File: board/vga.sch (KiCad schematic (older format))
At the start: 12 parts, among them P501 DE-15, P502 DE-15, U501 TCA9617A, U502 TCA9617A

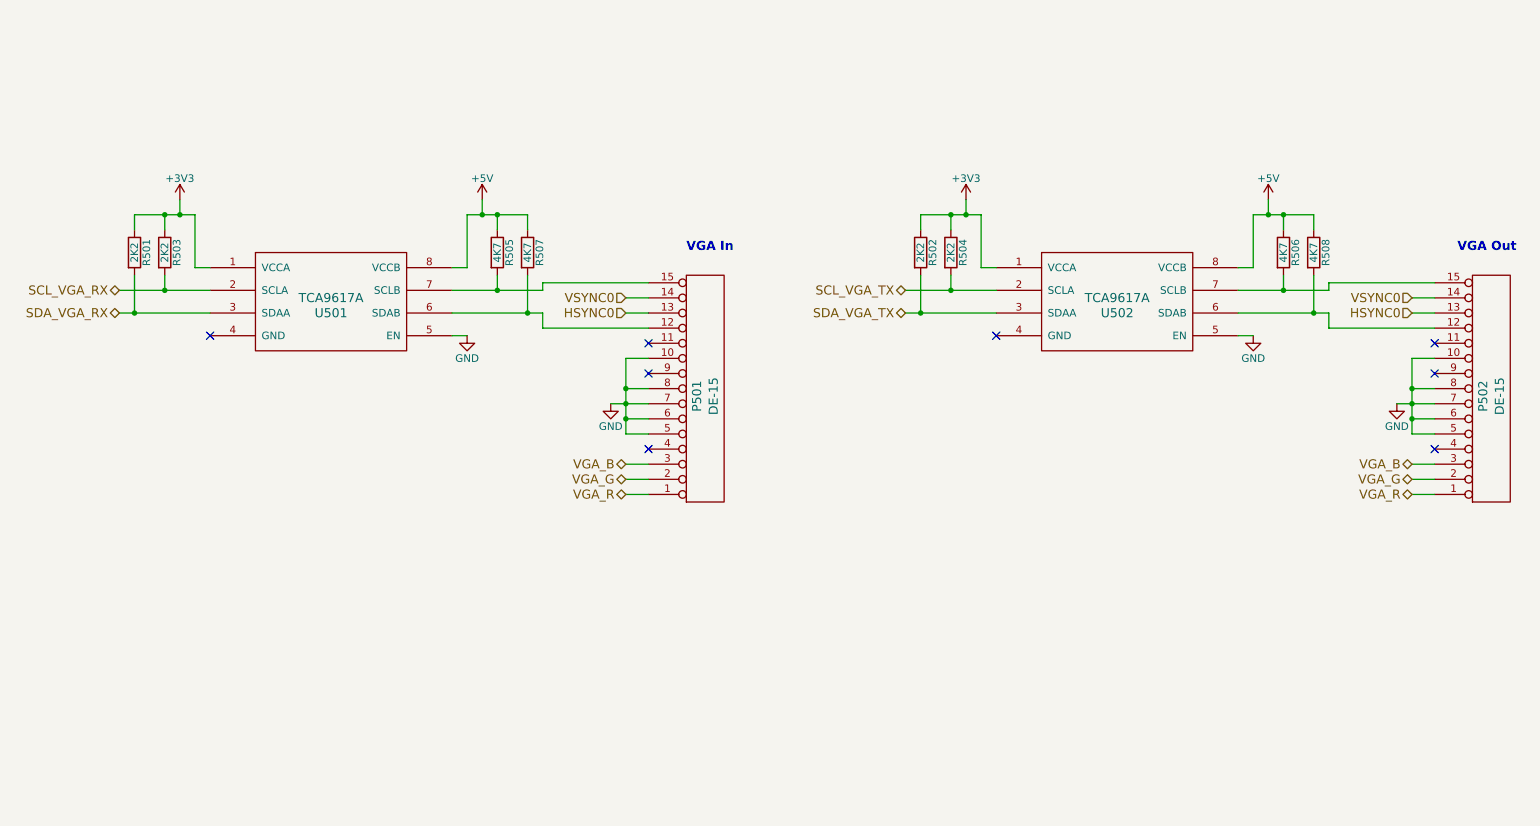
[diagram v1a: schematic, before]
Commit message: Added headers for the 4 I2C buses
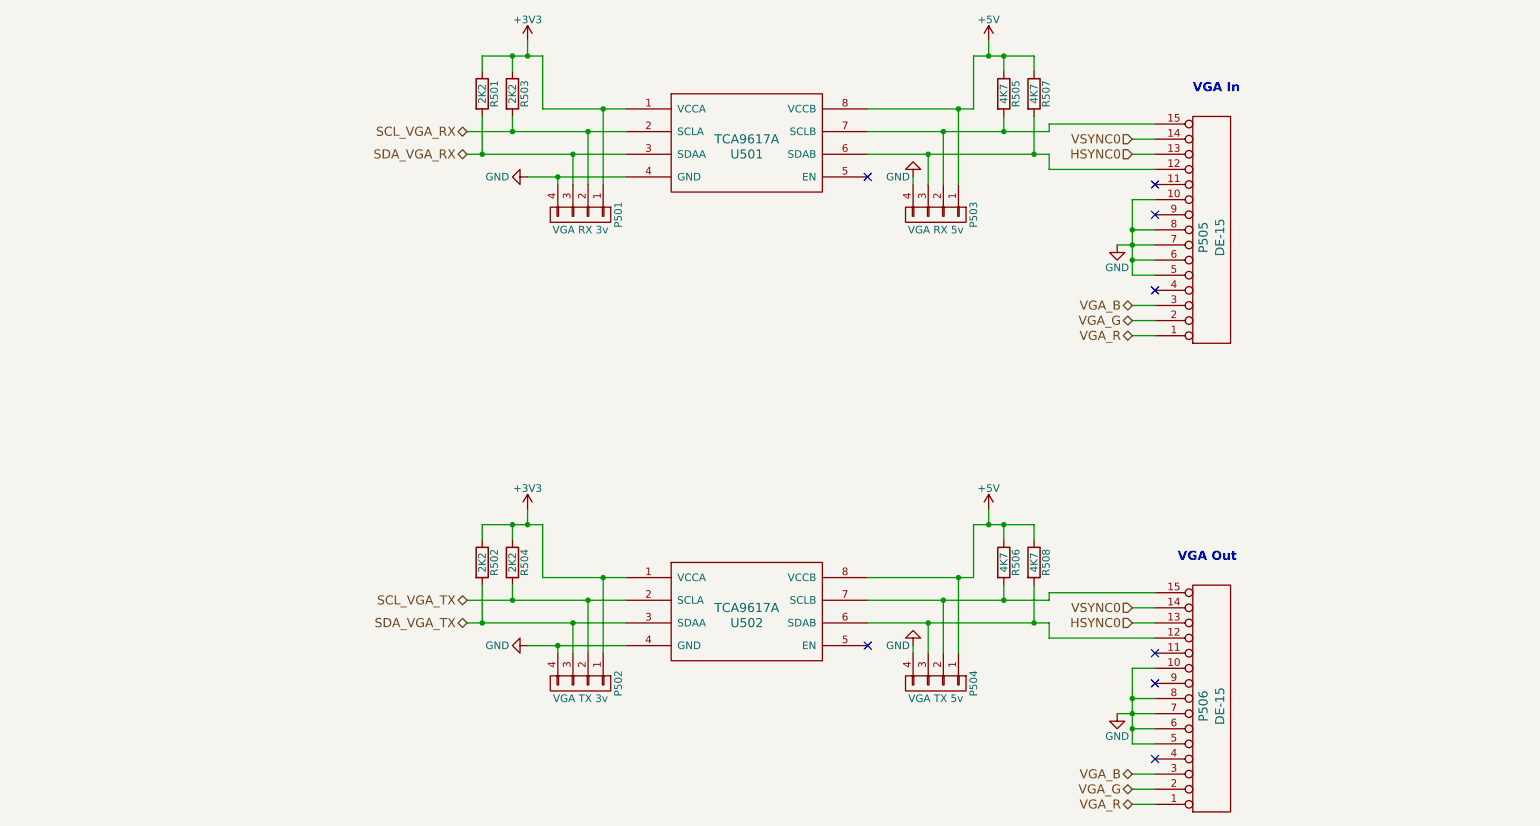
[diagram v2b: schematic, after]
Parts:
- added P501: VGA RX 3v, symbol CONN_01X04
- added P502: VGA TX 3v, symbol CONN_01X04
- added P503: VGA RX 5v, symbol CONN_01X04
- added P504: VGA TX 5v, symbol CONN_01X04
- renumbered P501 to P505, P502 to P506
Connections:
- net +3V3: now also P501.1 (P1), P502.1 (P1)
- net +5V: now also P503.1 (P1), P504.1 (P1)
- net GND: now also U501.4 (GND), U502.4 (GND), P501.4 (P4), P502.4 (P4), P503.4 (P4), P504.4 (P4); no longer U501.5 (EN), U502.5 (EN)
- net SCL_VGA_RX: now also P501.2 (P2)
- net SCL_VGA_TX: now also P502.2 (P2)
- net SDA_VGA_RX: now also P501.3 (P3)
- net SDA_VGA_TX: now also P502.3 (P3)
- net at P506.12 (P12), R508.2, U502.6 (SDAB): now also P504.3 (P3)
- net at P506.15 (P15), R506.2, U502.7 (SCLB): now also P504.2 (P2)
- net at P505.12 (P12), R507.2, U501.6 (SDAB): now also P503.3 (P3)
- net at P505.15 (P15), R505.2, U501.7 (SCLB): now also P503.2 (P2)
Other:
- moved on the sheet: P505, P506, R501, R502, R503, R504, R505, R506, R507, R508, U501, U502

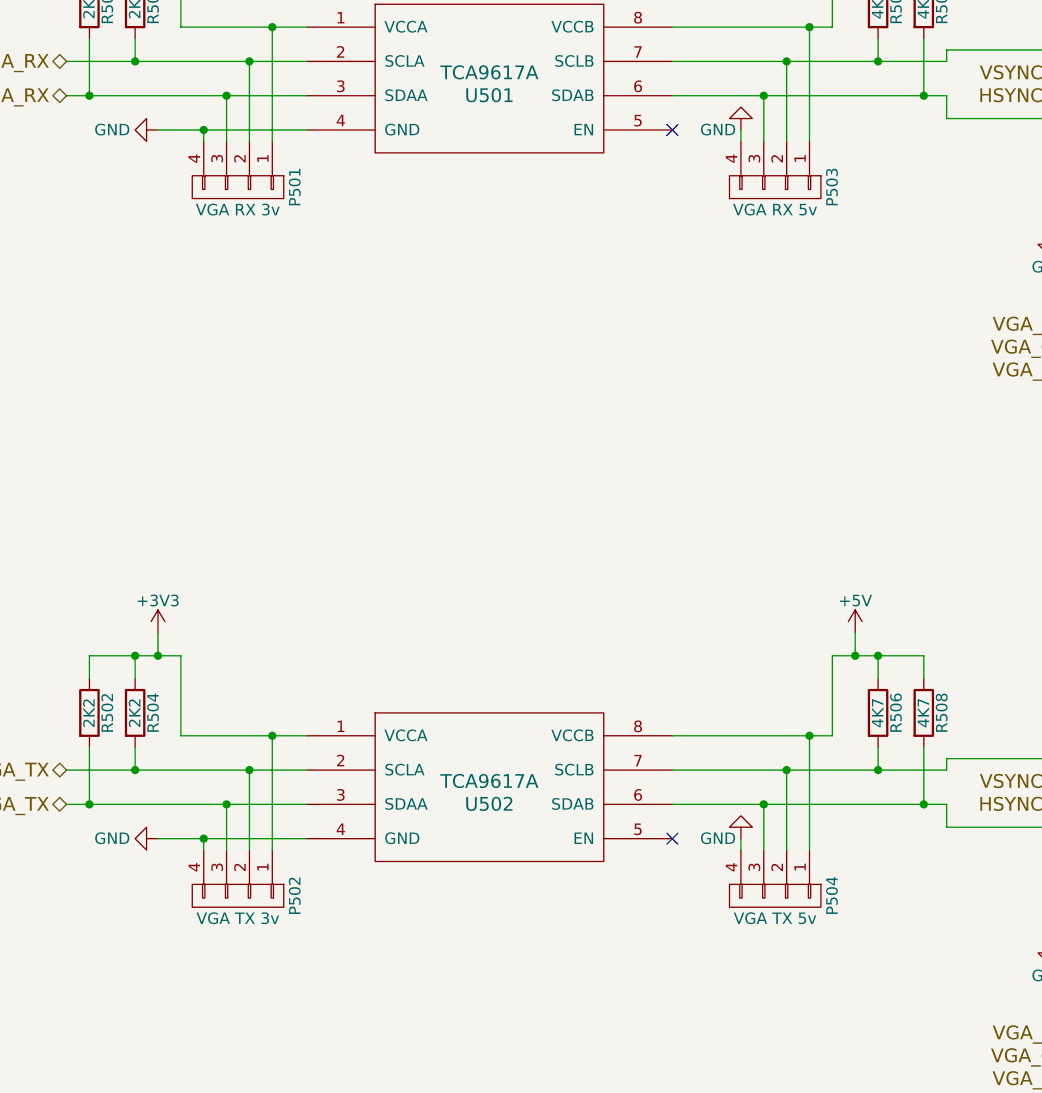
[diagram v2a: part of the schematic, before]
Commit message: Added I2C to the labels for I2C
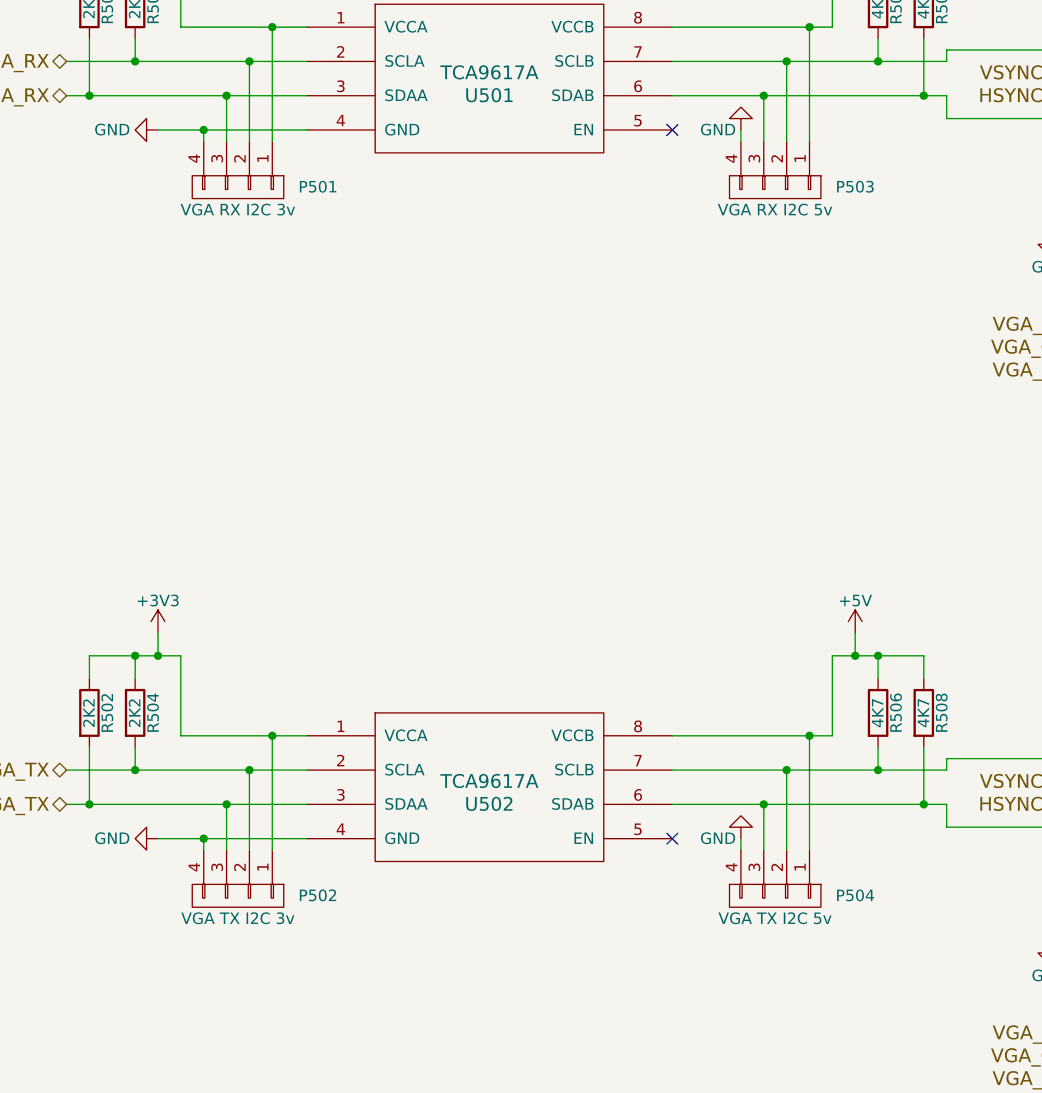
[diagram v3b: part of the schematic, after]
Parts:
- P501: value VGA RX 3v -> VGA RX I2C 3v
- P502: value VGA TX 3v -> VGA TX I2C 3v
- P503: value VGA RX 5v -> VGA RX I2C 5v
- P504: value VGA TX 5v -> VGA TX I2C 5v
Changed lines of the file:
@@
 U 1 1 5692AE99
 P 4650 2350
-F 0 "P501" H 4650 2600 50  0000 C CNN
-F 1 "VGA RX 3v" V 4750 2350 50  0000 C CNN
+F 0 "P501" V 4650 2700 50  0000 C CNN
+F 1 "VGA RX I2C 3v" V 4750 2350 50  0000 C CNN
 F 2 "" H 4650 2350 50  0000 C CNN
 F 3 "" H 4650 2350 50  0000 C CNN
@@
 U 1 1 5692BCA4
 P 4650 5450
-F 0 "P502" H 4650 5700 50  0000 C CNN
-F 1 "VGA TX 3v" V 4750 5450 50  0000 C CNN
+F 0 "P502" V 4650 5800 50  0000 C CNN
+F 1 "VGA TX I2C 3v" V 4750 5450 50  0000 C CNN
 F 2 "" H 4650 5450 50  0000 C CNN
 F 3 "" H 4650 5450 50  0000 C CNN
@@
 U 1 1 5692C534
 P 7000 2350
-F 0 "P503" H 7000 2600 50  0000 C CNN
-F 1 "VGA RX 5v" V 7100 2350 50  0000 C CNN
+F 0 "P503" V 7000 2700 50  0000 C CNN
+F 1 "VGA RX I2C 5v" V 7100 2350 50  0000 C CNN
 F 2 "" H 7000 2350 50  0000 C CNN
 F 3 "" H 7000 2350 50  0000 C CNN
@@
 U 1 1 5692D0C0
 P 7000 5450
-F 0 "P504" H 7000 5700 50  0000 C CNN
-F 1 "VGA TX 5v" V 7100 5450 50  0000 C CNN
+F 0 "P504" V 7000 5800 50  0000 C CNN
+F 1 "VGA TX I2C 5v" V 7100 5450 50  0000 C CNN
 F 2 "" H 7000 5450 50  0000 C CNN
 F 3 "" H 7000 5450 50  0000 C CNN

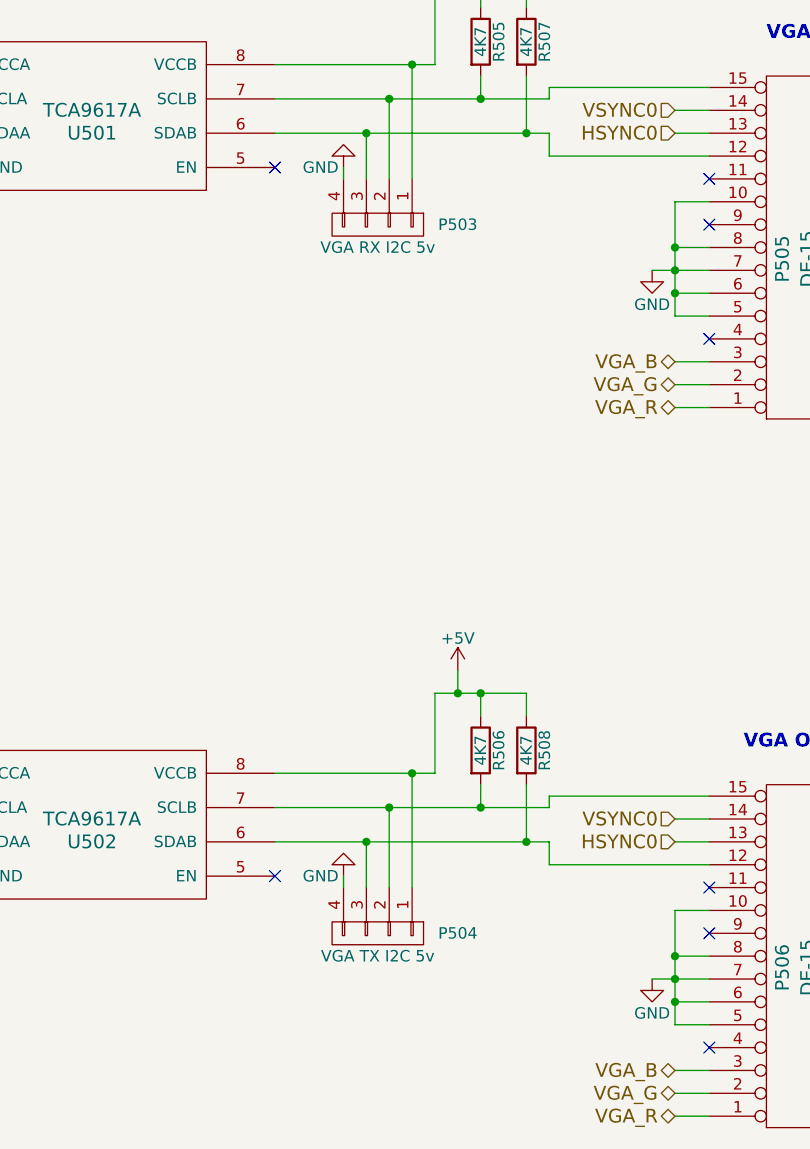
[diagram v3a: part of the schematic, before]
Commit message: Connect I2C level shifter EN to TOFE
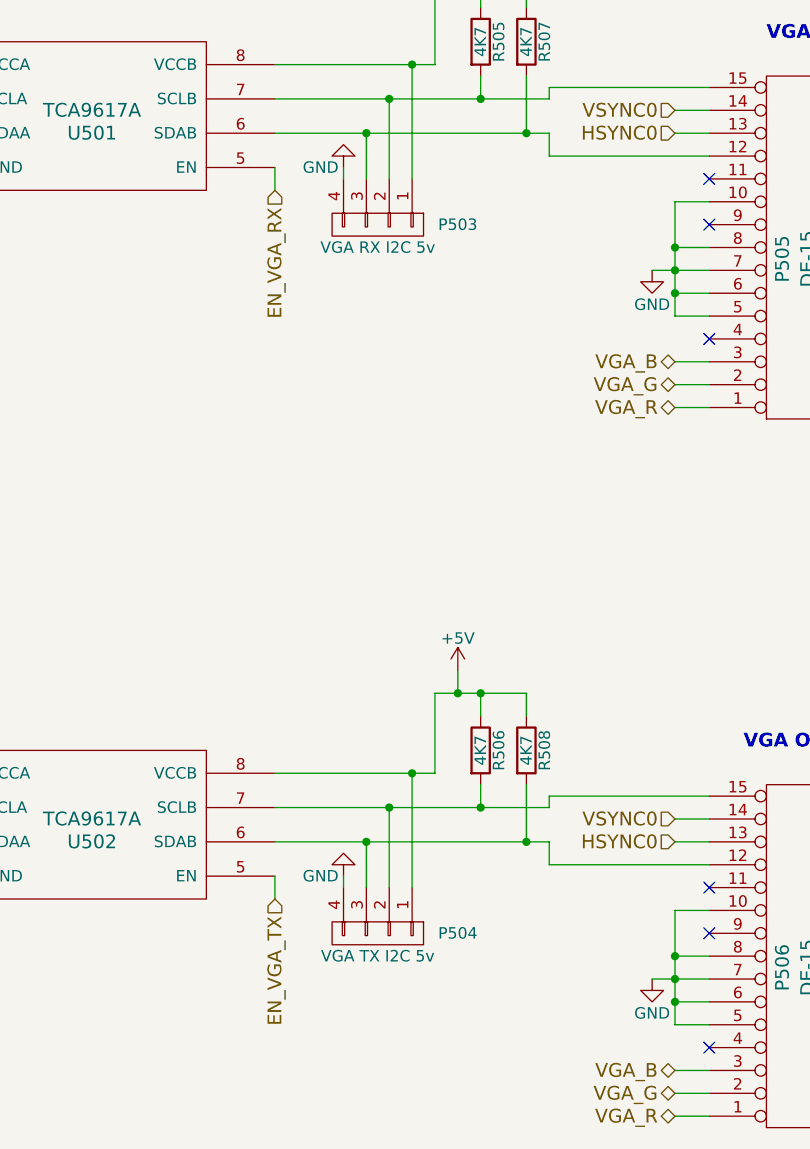
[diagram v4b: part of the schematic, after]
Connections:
- net EN_VGA_TX: now reaches U502.5 (EN)
- net EN_VGA_RX: now reaches U501.5 (EN)
- no-connect marks 8 -> 6
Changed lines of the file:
@@
 	1    0    0    -1
 $EndComp
-NoConn ~ 6550 5200
 Wire Wire Line
 	6550 4750 7250 4750
@@
 	7750 4850 7750 4900
 Wire Wire Line
-	7750 5050 7750 5150
+	7750 5150 7750 5050
 Text HLabel 8300 6050 0    60   BiDi ~ 0
 VGA_B
@@
 	7750 4900 6550 4900
 Wire Wire Line
-	6550 5050 7750 5050
+	7750 5050 6550 5050
 Wire Wire Line
 	7650 4800 7650 5050
@@
 	1    0    0    -1
 $EndComp
-NoConn ~ 6550 2100
 Wire Wire Line
 	6550 1650 7250 1650
@@
 Connection ~ 7050 4900
 Connection ~ 6950 5050
+Text HLabel 6550 2200 3    60   Input ~ 0
+EN_VGA_RX
+Wire Wire Line
+	6550 2100 6550 2200
+Text HLabel 6550 5300 3    60   Input ~ 0
+EN_VGA_TX
+Wire Wire Line
+	6550 5300 6550 5200
 $EndSCHEMATC
